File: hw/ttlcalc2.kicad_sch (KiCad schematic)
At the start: 52 parts, among them J1 POWER, J2 RST, J3 IO_BUS, J4 EXT_CLK, J5 CLK_SRC, U1 74LS163, U10 74LS273, U11 74LS273, U12 74LS283, U13 74LS08, U14 74LS138, U15 74LS138, U16 74LS04, U17 74LS08, U18 74LS151, U19 74LS191, U2 74LS163, U20 74LS191, U21 74LS157, U22 74LS08, U23 74LS173, U24 74LS244, U25 74LS173, U26 2101, U27 74LS157, U28 74LS173, U29 74LS244, U3 74LS163, U30 74LS244, U31 74LS244, U32 74LS73, U33 74LS00, U34 74LS73, U35 74LS373, U4 74LS173, U5 74LS173, U6 27C64, U7 27C64, U8 74LS181, U9 74LS283, X1 TCXO3

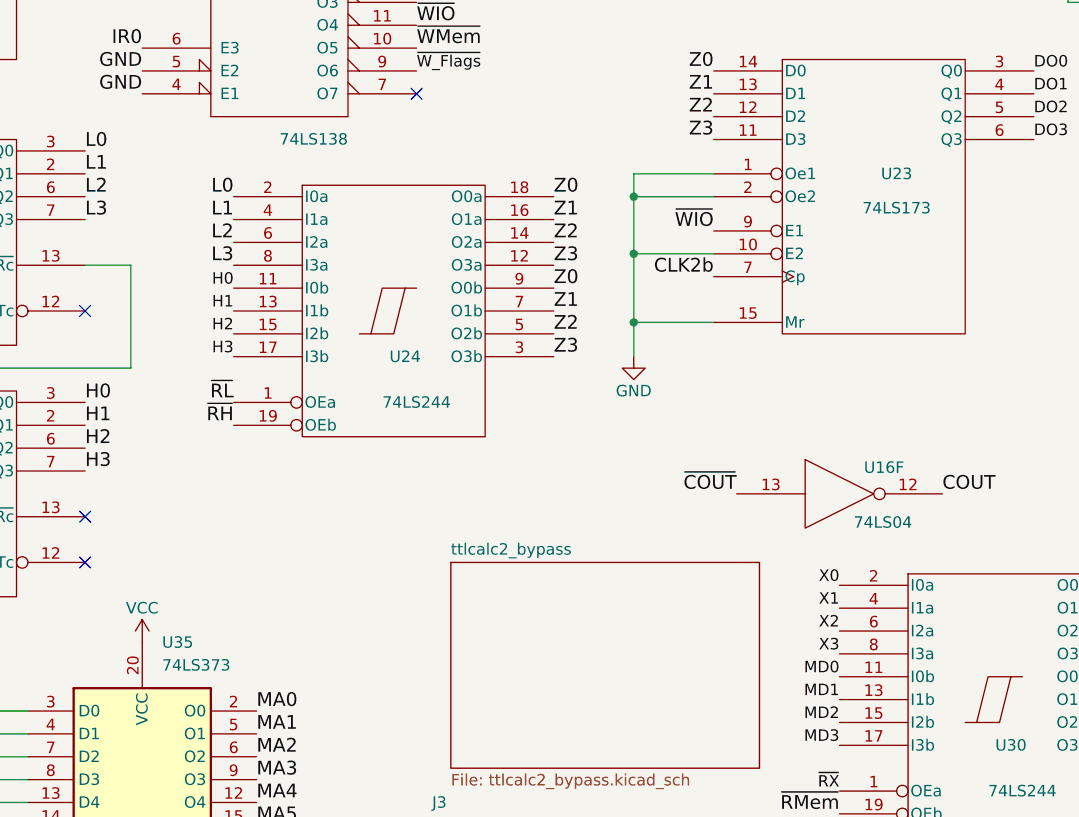
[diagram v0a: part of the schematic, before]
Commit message: PCB cleanup
Swap location of I/O output register and address latch
Clean up routing
Via stitch around clock traces
Fill out sheet description block
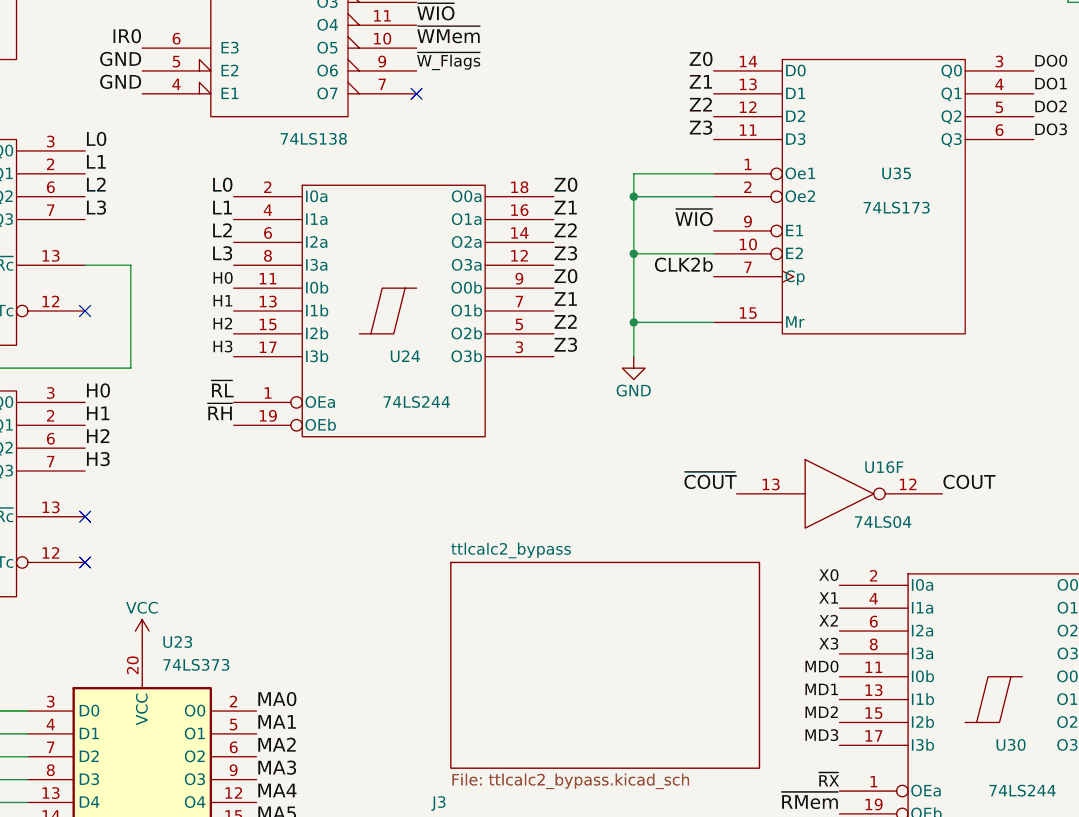
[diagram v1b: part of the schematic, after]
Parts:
- renumbered U35 to U23, U23 to U35
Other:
- title: (none) -> TTL Calculator Logic Board
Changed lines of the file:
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@@
 	(generator_version "8.0")
 	(paper "USLedger")
+	(title_block
+		(title "TTL Calculator Logic Board")
+		(date "2025-02-12")
+		(rev "B")
+	)
 	(junction
 		(at 162.56 213.36)
@@
 		(on_board yes)
 		(dnp no)
-		(property "Reference" "U23"
+		(property "Reference" "U35"
 			(at 201.93 134.62 0)
 			(effects
@@
 			(project "ttlcalc2"
 				(path "/3b710599-b9c0-4419-afaf-5ca10da300b4"
-					(reference "U23")
+					(reference "U35")
 					(unit 1)
 				)
@@
 		(dnp no)
 		(fields_autoplaced yes)
-		(property "Reference" "U35"
+		(property "Reference" "U23"
 			(at 120.3041 186.69 0)
 			(effects
@@
 			(project ""
 				(path "/3b710599-b9c0-4419-afaf-5ca10da300b4"
-					(reference "U35")
+					(reference "U23")
 					(unit 1)
 				)
